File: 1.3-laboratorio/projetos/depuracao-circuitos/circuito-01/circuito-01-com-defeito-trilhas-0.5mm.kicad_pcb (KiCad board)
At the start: 2 copper layers, 76.2 x 54.6 mm, 26 parts, among them J1 Conn_01x07_Male, J2 Conn_01x07_Male, J3 Conn_01x07_Male, J4 Conn_01x07_Male, J5 Conn_01x07_Male, J6 Conn_01x07_Male, J7 Conn_01x05, J8 Conn_01x05, P1 CONN_01X02, SW1 SW_DIP_x04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

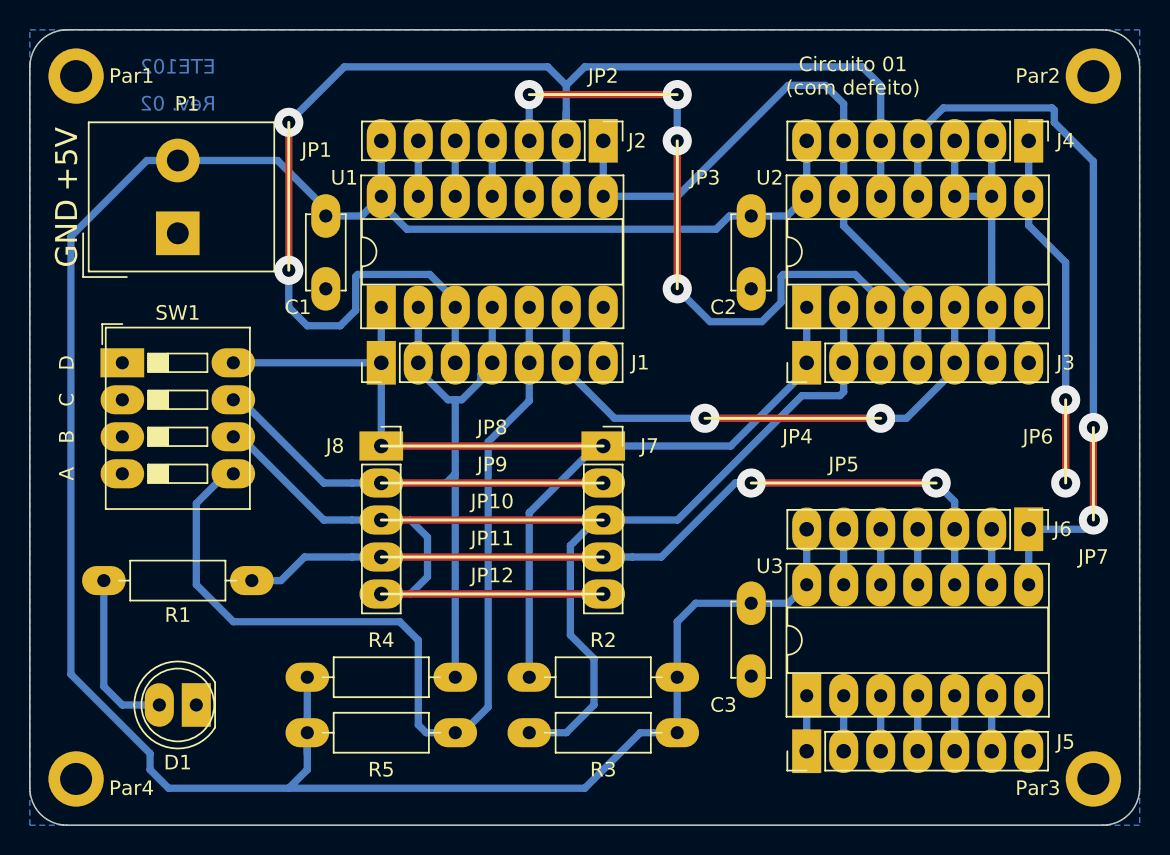
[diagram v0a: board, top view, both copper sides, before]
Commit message: Troca do 74LS386 pelo 74LS86 e correspondentes ajustes no esquemático e na PCI.
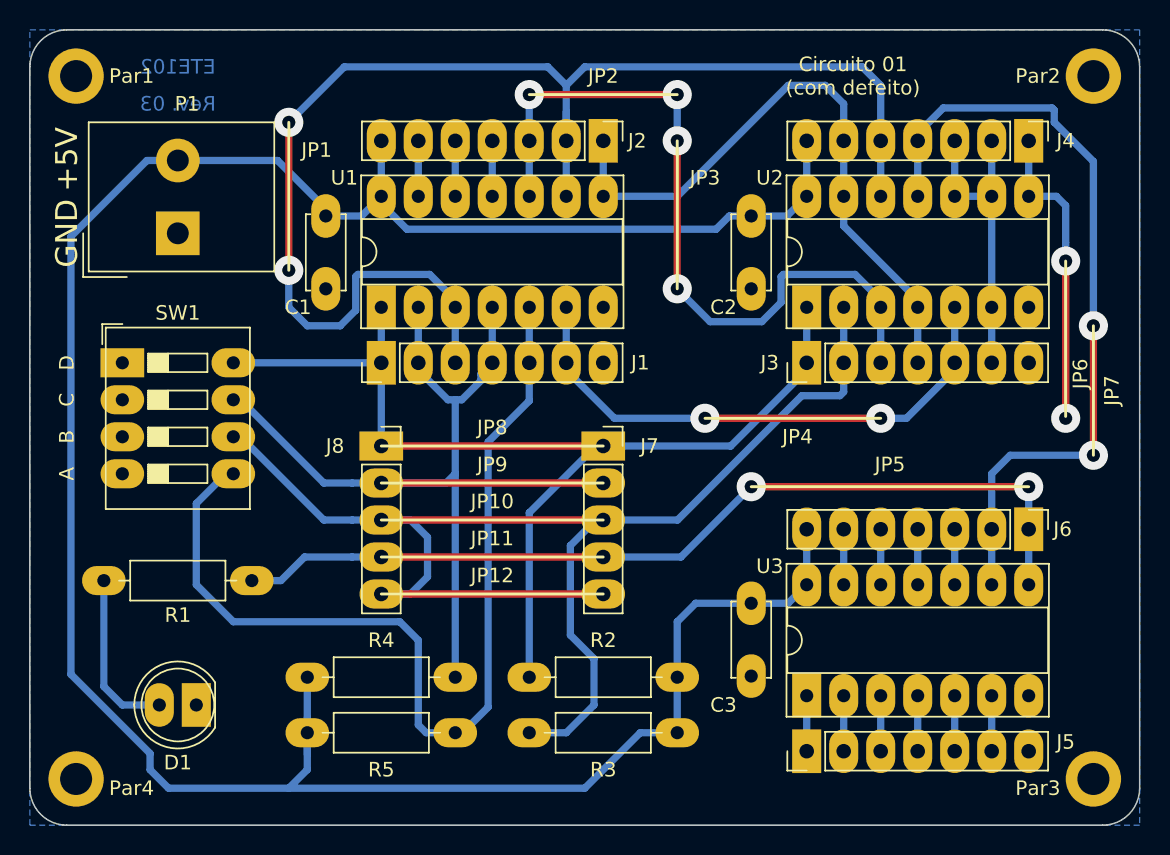
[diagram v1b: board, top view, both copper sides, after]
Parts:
- U3: value 74LS386 -> 74LS86
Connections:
- J6 pad 1: /U2-11 -> /U3-08
- J6 pad 2: /U3-09 -> /U2-11
- J7 pad 4: /U3-10 -> /U3-08
- J8 pad 4: /U3-10 -> /U3-08
- R1 pad 1: /U3-10 -> /U3-08
- U3 pad 8: /U2-11 -> /U3-08
- U3 pad 9: /U3-09 -> /U2-11
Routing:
- net /U3-08: track 0.00 -> 63.0 mm, vias 0 -> 2
- net /U3-10: track 57.3 -> 3.81 mm, vias 2 -> 0
- net /U3-09: track 3.81 -> 0.00 mm
- net /U2-08: track 24.5 -> 21.2 mm
- net /U2-11: track 52.3 -> 54.4 mm
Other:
- board text added: "Rev. 03"
- board text removed: "Rev. 02"

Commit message: Alteração de trilha para provocar curto intencional na variável 'B' ao invés da 'C', pois esta não influencia na saída.
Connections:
- J8 pad 5: /U2-02 -> /U1-02
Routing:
- net /U2-02: track 84.1 -> 74.1 mm
- net /U1-02: track 67.5 -> 72.9 mm
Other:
- board text added: "Rev. 04"
- board text removed: "Rev. 03"
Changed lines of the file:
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@@
-(kicad_pcb (version 20171130) (host pcbnew "(5.0.2)-1")
+(kicad_pcb (version 20171130) (host pcbnew 5.0.2-bee76a0~70~ubuntu16.04.1)
   (general
     (thickness 1.6)
     (drawings 56)
-    (tracks 227)
+    (tracks 225)
     (zones 0)
     (modules 26)
@@
       (linewidth 0.100000)
       (plotframeref false)
-      (viasonmask false)
+      (viasonmask true)
       (mode 1)
       (useauxorigin false)
@@
     (fp_line (start -1.27 -1.27) (end 0.635 -1.27) (layer F.Fab) (width 0.1))
     (pad 5 thru_hole oval (at 0 10.16) (size 3 2) (drill 1) (layers *.Cu *.Mask)
-      (net 17 /U2-02))
+      (net 16 /U1-02))
     (pad 4 thru_hole oval (at 0 7.62) (size 3 2) (drill 1) (layers *.Cu *.Mask)
       (net 28 /U3-08))
@@
     (effects (font (size 1 1) (thickness 0.15)))
   )
-  (gr_text "Rev. 03" (at 118.11 74.93) (layer B.Cu)
+  (gr_text "Rev. 04" (at 118.11 74.93) (layer B.Cu)
     (effects (font (size 1 1) (thickness 0.2)) (justify mirror))
   )
@@
   (segment (start 173.99 100.33) (end 175.26 99.06) (width 0.5) (layer B.Cu) (net 11))
   (segment (start 171.45 107.95) (end 171.45 104.14) (width 0.5) (layer B.Cu) (net 12))
-  (segment (start 132.08 106.045) (end 147.32 106.045) (width 0.5) (layer F.Cu) (net 28))
-  (segment (start 130.08 106.045) (end 132.08 106.045) (width 0.5) (layer B.Cu) (net 28))
-  (segment (start 126.81 106.045) (end 130.08 106.045) (width 0.5) (layer B.Cu) (net 28))
-  (segment (start 125.19 107.665) (end 126.81 106.045) (width 0.5) (layer B.Cu) (net 28))
-  (segment (start 123.19 107.665) (end 125.19 107.665) (width 0.5) (layer B.Cu) (net 28))
-  (via (at 157.48 101.219) (size 2) (drill 0.9) (layers F.Cu B.Cu) (net 28))
   (segment (start 168.91 107.95) (end 168.91 104.14) (width 0.5) (layer B.Cu) (net 13) (status 30))
   (segment (start 166.37 104.14) (end 166.37 107.95) (width 0.5) (layer B.Cu) (net 14) (status 30))
@@
   (segment (start 132.08 100.965) (end 136.525 100.965) (width 0.5) (layer B.Cu) (net 16))
   (segment (start 137.16 95.25) (end 137.16 100.33) (width 0.5) (layer B.Cu) (net 16))
-  (segment (start 137.16 100.33) (end 137.16 114.3) (width 0.5) (layer B.Cu) (net 16))
+  (segment (start 132.08 108.585) (end 136.525 108.585) (width 0.5) (layer B.Cu) (net 16))
+  (segment (start 136.525 108.585) (end 137.16 107.95) (width 0.5) (layer B.Cu) (net 16))
+  (segment (start 137.16 107.95) (end 137.16 114.3) (width 0.5) (layer B.Cu) (net 16))
+  (segment (start 137.16 100.33) (end 137.16 107.95) (width 0.5) (layer B.Cu) (net 16))
   (segment (start 163.83 92.71) (end 163.83 88.9) (width 0.5) (layer B.Cu) (net 17) (status 30))
   (segment (start 147.32 103.505) (end 132.08 103.505) (width 0.5) (layer F.Cu) (net 17))
@@
   (segment (start 147.32 103.505) (end 152.420541 103.505) (width 0.5) (layer B.Cu) (net 17))
   (segment (start 152.420541 103.505) (end 160.957539 94.968001) (width 0.5) (layer B.Cu) (net 17))
-  (segment (start 134.08 108.585) (end 132.08 108.585) (width 0.5) (layer B.Cu) (net 17))
-  (segment (start 135.255 107.41) (end 134.08 108.585) (width 0.5) (layer B.Cu) (net 17))
-  (segment (start 135.255 104.68) (end 135.255 107.41) (width 0.5) (layer B.Cu) (net 17))
-  (segment (start 134.08 103.505) (end 135.255 104.68) (width 0.5) (layer B.Cu) (net 17))
-  (segment (start 132.08 103.505) (end 134.08 103.505) (width 0.5) (layer B.Cu) (net 17))
   (segment (start 142.24 88.9) (end 142.24 92.71) (width 0.5) (layer B.Cu) (net 18) (status 30))
   (segment (start 136.66 118.11) (end 137.16 118.11) (width 0.5) (layer B.Cu) (net 18) (status 30))
@@
   (segment (start 163.83 119.38) (end 163.83 115.57) (width 0.5) (layer B.Cu) (net 26) (status 30))
   (segment (start 161.29 115.57) (end 161.29 119.38) (width 0.5) (layer B.Cu) (net 27) (status 30))
+  (segment (start 132.08 106.045) (end 147.32 106.045) (width 0.5) (layer F.Cu) (net 28))
+  (segment (start 130.08 106.045) (end 132.08 106.045) (width 0.5) (layer B.Cu) (net 28))
+  (segment (start 126.81 106.045) (end 130.08 106.045) (width 0.5) (layer B.Cu) (net 28))
+  (segment (start 125.19 107.665) (end 126.81 106.045) (width 0.5) (layer B.Cu) (net 28))
+  (segment (start 123.19 107.665) (end 125.19 107.665) (width 0.5) (layer B.Cu) (net 28))
+  (via (at 157.48 101.219) (size 2) (drill 0.9) (layers F.Cu B.Cu) (net 28))
   (segment (start 176.53 107.95) (end 176.53 104.14) (width 0.5) (layer B.Cu) (net 28))
   (segment (start 176.53 101.219) (end 157.48 101.219) (width 0.5) (layer F.Cu) (net 28))

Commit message: Observações quanto aos testes que haviam sido realizados para a Ponta de Prova Lógica e para o Circuito para Depuração 01.
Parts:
- D1: value LED_ALT -> LED_VM
